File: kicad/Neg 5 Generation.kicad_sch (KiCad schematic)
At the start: 4 parts, among them T1 10uF, T2 10uF, U5 LMC7660

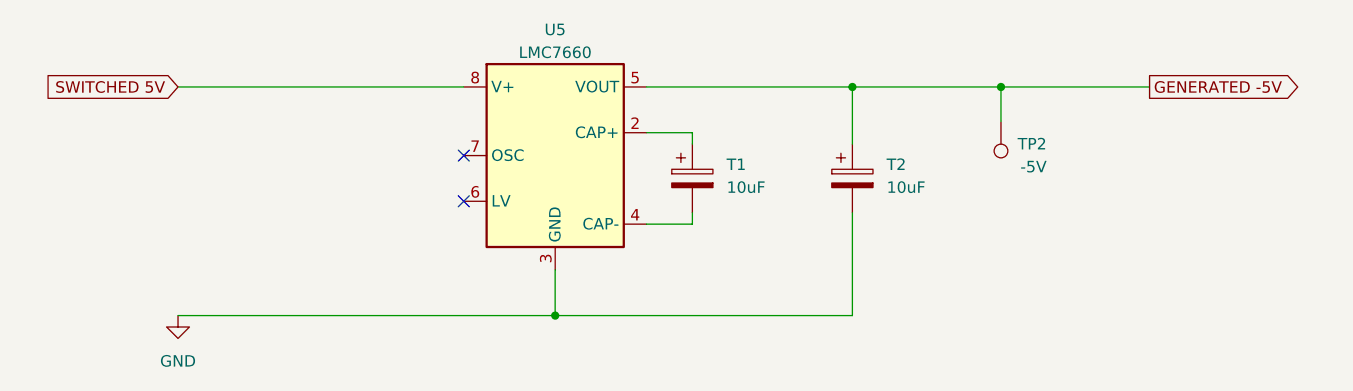
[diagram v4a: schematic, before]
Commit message: Kicad 8, updated docs
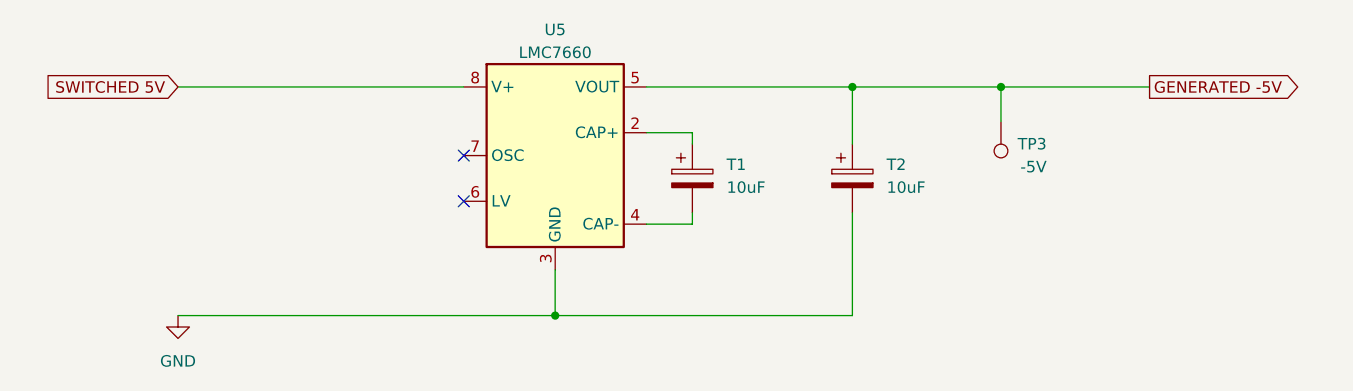
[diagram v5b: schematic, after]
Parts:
- renumbered TP2 to TP3
